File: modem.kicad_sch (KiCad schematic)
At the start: 14 parts, among them J1 2337019-1, J2 2337019-1, U1 BG95MxLA

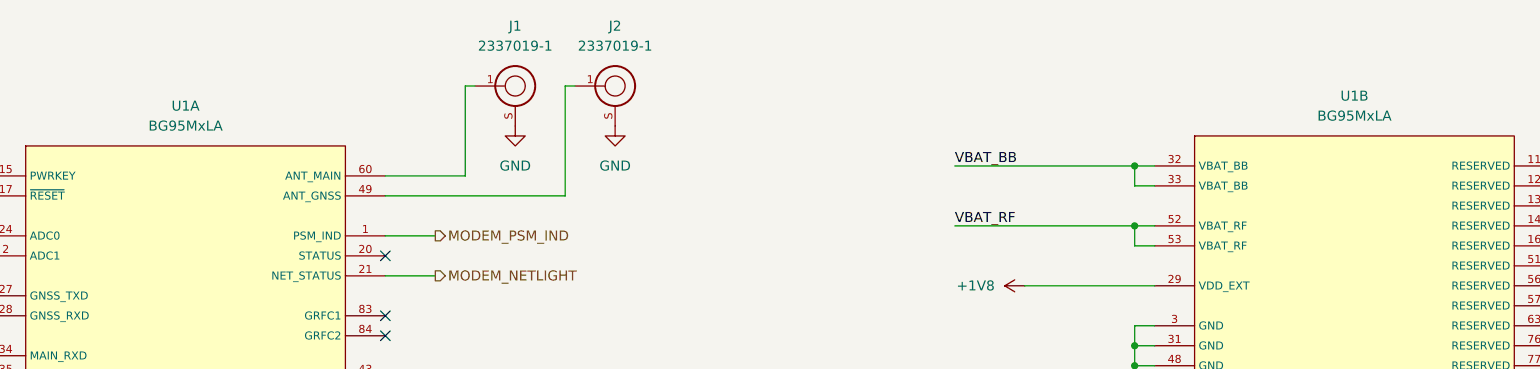
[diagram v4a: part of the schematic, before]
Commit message: Move to NSIM-16-B sim card holder for easier sourcing
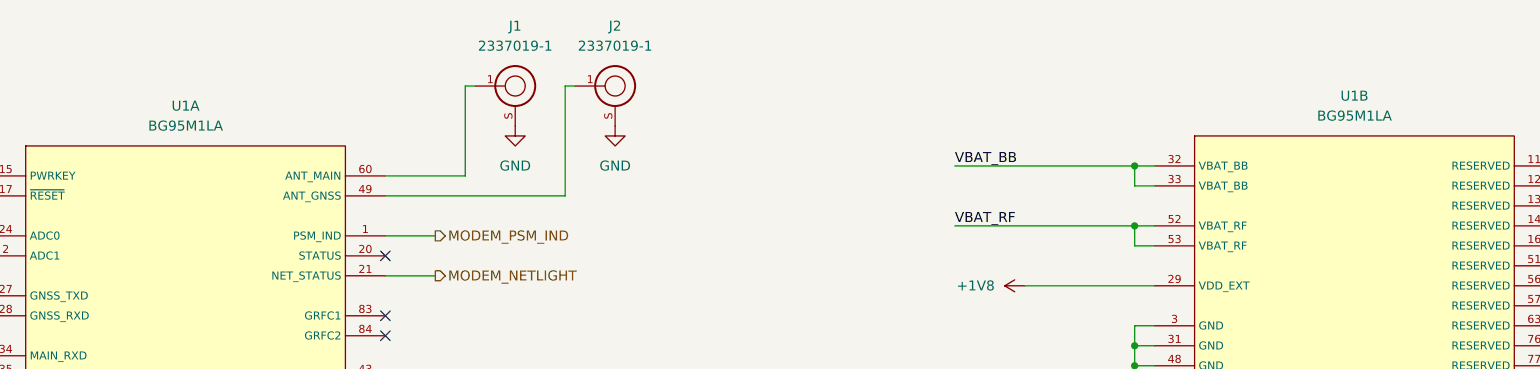
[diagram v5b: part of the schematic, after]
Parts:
- J1, J2: footprint J_Connector:A-1JB -> J_Connector:U.FL
- U1: value BG95MxLA -> BG95M1LA
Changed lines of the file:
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@@
 	)
 	(symbol
+		(lib_name "2337019-1_1")
 		(lib_id "J_Connector:2337019-1")
 		(at 125.73 30.48 0)
@@
 			)
 		)
-		(property "Footprint" "J_Connector:A-1JB"
+		(property "Footprint" "J_Connector:U.FL"
 			(at 125.73 41.91 0)
 			(effects
@@
 			)
 		)
-		(property "Value" "BG95MxLA"
+		(property "Value" "BG95M1LA"
 			(at 232.41 34.29 0)
 			(effects
@@
 			)
 		)
-		(property "Footprint" "J_Connector:A-1JB"
+		(property "Footprint" "J_Connector:U.FL"
 			(at 138.43 41.91 0)
 			(effects
@@
 			)
 		)
-		(property "Value" "BG95MxLA"
+		(property "Value" "BG95M1LA"
 			(at 83.82 35.56 0)
 			(effects
